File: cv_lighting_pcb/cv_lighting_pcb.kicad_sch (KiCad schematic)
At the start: 27 parts, among them Q1 2N3906, U1 Current Driver, U2 Camera Input, U3 VO617A, U4 Barrel Jack

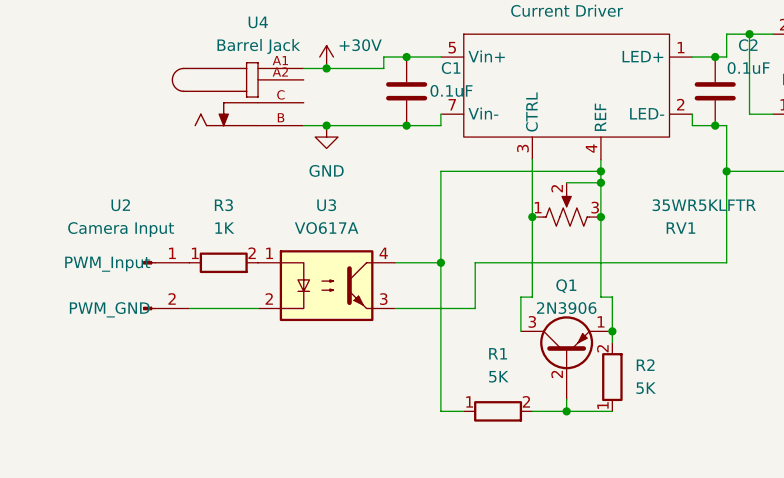
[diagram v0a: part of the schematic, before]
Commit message: added some notes to schematic
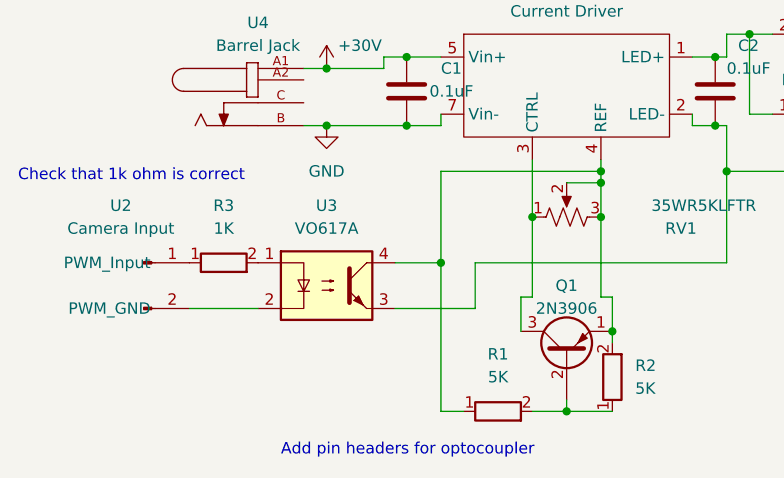
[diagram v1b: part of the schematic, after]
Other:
- note added: "Add pin headers for optocoupler"
- note added: "Check that 1k ohm is correct"
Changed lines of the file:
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@@
     (stroke (width 0) (type default))
+  )
+  (text "Check that 1k ohm is correct" (at 45.72 113.03 0)
+    (effects (font (size 1.27 1.27)) (justify left bottom))
+  )
+  (text "Add pin headers for optocoupler\n" (at 74.93 143.51 0)
+    (effects (font (size 1.27 1.27)) (justify left bottom))
   )
   (text "Control dimming: optocoupler or something\nSo far this circuit has 8 leds and one current driver"

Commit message: Added some changes
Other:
- company: (none) -> Illini Pacbot Team
- title: (none) -> Lighting PCB
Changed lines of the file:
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@@
 (kicad_sch (version 20230121) (generator eeschema)
   (paper "A4")
+  (title_block
+    (title "Lighting PCB")
+    (date "2023-12-02")
+    (company "Illini Pacbot Team")
+  )
   (junction (at 177.8 96.52) (diameter 0) (color 0 0 0 0)
   )

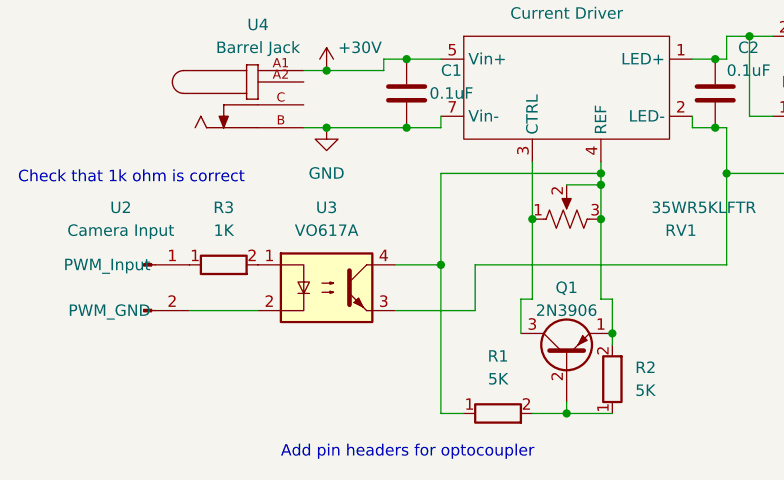
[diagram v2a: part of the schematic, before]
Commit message: more changes to lighting pcb
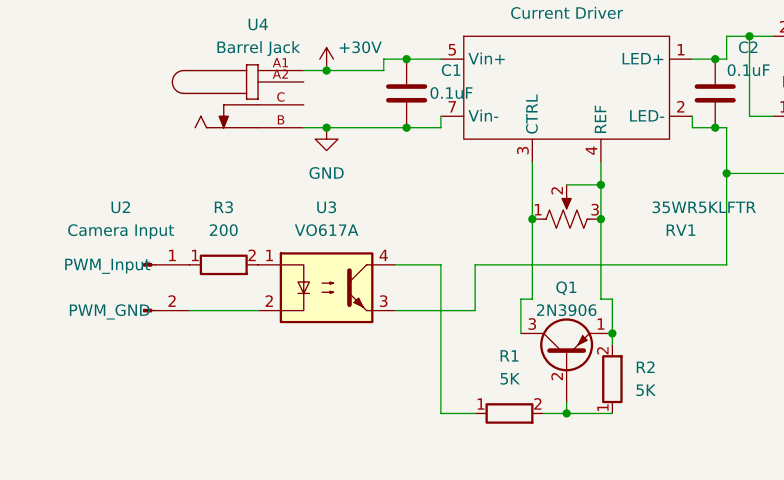
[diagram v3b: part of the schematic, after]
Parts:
- R3: value 1K -> 200
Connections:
- net at Q1.1 (E), R2.2, RV1.2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: no longer R1.1, U3.4
- new net: R1.1, U3.4
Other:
- note removed: "Add pin headers for optocoupler"
- note removed: "Check that 1k ohm is correct"
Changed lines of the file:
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@@
   (junction (at 203.2 105.41) (diameter 0) (color 0 0 0 0)
   )
-  (junction (at 92.71 121.92) (diameter 0) (color 0 0 0 0)
-  )
   (junction (at 152.4 105.41) (diameter 0) (color 0 0 0 0)
   )
-  (junction (at 110.49 111.76) (diameter 0) (color 0 0 0 0)
-  )
   (junction (at 139.7 105.41) (diameter 0) (color 0 0 0 0)
   )
@@
     (stroke (width 0) (type default))
   )
+  (wire (pts (xy 92.71 138.43) (xy 96.52 138.43))
+    (stroke (width 0) (type default))
+  )
   (wire (pts (xy 106.68 138.43) (xy 111.76 138.43))
     (stroke (width 0) (type default))
@@
     (stroke (width 0) (type default))
   )
-  (wire (pts (xy 92.71 111.76) (xy 110.49 111.76))
-    (stroke (width 0) (type default))
-  )
   (wire (pts (xy 80.01 100.33) (xy 86.36 100.33))
     (stroke (width 0) (type default))
@@
     (stroke (width 0) (type default))
   )
-  (wire (pts (xy 92.71 111.76) (xy 92.71 121.92))
-    (stroke (width 0) (type default))
-  )
-  (wire (pts (xy 92.71 138.43) (xy 95.25 138.43))
-    (stroke (width 0) (type default))
-  )
   (wire (pts (xy 203.2 96.52) (xy 203.2 105.41))
     (stroke (width 0) (type default))
   )
-  (wire (pts (xy 110.49 110.49) (xy 110.49 111.76))
-    (stroke (width 0) (type default))
-  )
   (wire (pts (xy 106.68 137.16) (xy 106.68 138.43))
     (stroke (width 0) (type default))
@@
     (stroke (width 0) (type default))
   )
+  (wire (pts (xy 104.14 138.43) (xy 106.68 138.43))
+    (stroke (width 0) (type default))
+  )
   (wire (pts (xy 64.77 127) (xy 72.39 127))
     (stroke (width 0) (type default))
@@
     (stroke (width 0) (type default))
   )
-  (wire (pts (xy 110.49 111.76) (xy 110.49 113.03))
+  (wire (pts (xy 110.49 110.49) (xy 110.49 113.03))
     (stroke (width 0) (type default))
   )
@@
     (stroke (width 0) (type default))
   )
-  (wire (pts (xy 106.68 138.43) (xy 102.87 138.43))
-    (stroke (width 0) (type default))
-  )
   (wire (pts (xy 227.33 96.52) (xy 227.33 105.41))
     (stroke (width 0) (type default))
@@
   (wire (pts (xy 139.7 105.41) (xy 142.24 105.41))
     (stroke (width 0) (type default))
-  )
-  (text "Check that 1k ohm is correct" (at 45.72 113.03 0)
-    (effects (font (size 1.27 1.27)) (justify left bottom))
-  )
-  (text "Add pin headers for optocoupler\n" (at 74.93 143.51 0)
-    (effects (font (size 1.27 1.27)) (justify left bottom))
   )
   (text "Control dimming: optocoupler or something\nSo far this circuit has 8 leds and one current driver"
     (at 90.17 85.09 0)
     (effects (font (size 1.27 1.27)) (justify left bottom))
+  )
+  (symbol (lib_name "R_1") (lib_id "Device:R") (at 100.33 138.43 90) (unit 1)
+    (in_bom yes) (on_board yes) (dnp no) (fields_autoplaced)
+    (property "Reference" "R1" (at 100.33 132.08 90)
+      (effects (font (size 1.27 1.27)))
+    )
+    (property "Value" "5K" (at 100.33 134.62 90)
+      (effects (font (size 1.27 1.27)))
+    )
+    (property "Footprint" "Resistor_SMD:R_0805_2012Metric_Pad1.20x1.40mm_HandSolder" (at 100.33 140.208 90)
+      (effects (font (size 1.27 1.27)) hide)
+    )
+    (property "Datasheet" "~" (at 100.33 138.43 0)
+      (effects (font (size 1.27 1.27)) hide)
+    )
+    (pin "1")
+    (pin "2")
+    (instances
+      (project "cv_lighting_pcb"
+        (path "/d003750a-5843-4e2f-8a13-c4462072ff66"
+          (reference "R1") (unit 1)
+        )
+      )
+    )
   )
   (symbol (lib_name "LED_1") (lib_id "Device:LED") (at 133.35 96.52 180) (unit 1)
@@
       (effects (font (size 1.27 1.27)))
     )
-    (property "Value" "1K" (at 68.58 118.11 90)
+    (property "Value" "200" (at 68.58 118.11 90)
       (effects (font (size 1.27 1.27)))
     )
@@
         )
       )
-    )
-  )
-  (symbol (lib_name "R_2") (lib_id "Device:R") (at 99.06 138.43 90) (unit 1)
-    (in_bom yes) (on_board yes) (dnp no)
-    (property "Reference" "R1" (at 99.06 132.08 90)
-      (effects (font (size 1.27 1.27)))
-    )
-    (property "Value" "5K" (at 99.06 134.62 90)
-      (effects (font (size 1.27 1.27)))
-    )
-    (property "Footprint" "Resistor_SMD:R_0805_2012Metric_Pad1.20x1.40mm_HandSolder" (at 99.06 140.208 90)
-      (effects (font (size 1.27 1.27)) hide)
-    )
-    (property "Datasheet" "~" (at 99.06 138.43 0)
-      (effects (font (size 1.27 1.27)) hide)
-    )
-    (pin "1")
-    (pin "2")
-    (instances
-      (project "cv_lighting_pcb"
-        (path "/d003750a-5843-4e2f-8a13-c4462072ff66"
-          (reference "R1") (unit 1)
-        )
-      )
